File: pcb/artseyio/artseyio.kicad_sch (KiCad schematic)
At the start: 17 parts, among them J1 USB_C16PIN, J2 RST, SW1 SW_MEC_5G, SW2 SW_MEC_5G, SW3 SW_MEC_5G, SW4 SW_MEC_5G, SW5 SW_MEC_5G, SW6 SW_MEC_5G, SW7 SW_MEC_5G, SW8 SW_MEC_5G, U3 CH552G

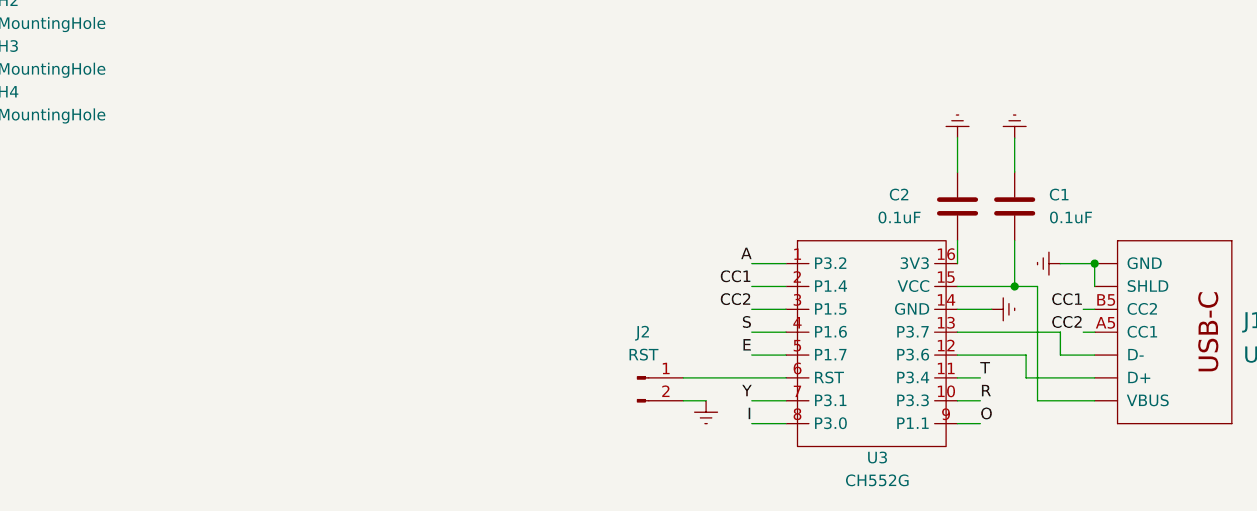
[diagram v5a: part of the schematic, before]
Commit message: Filled out v1.1 design with boot jumper and correct cc line pulldowns.
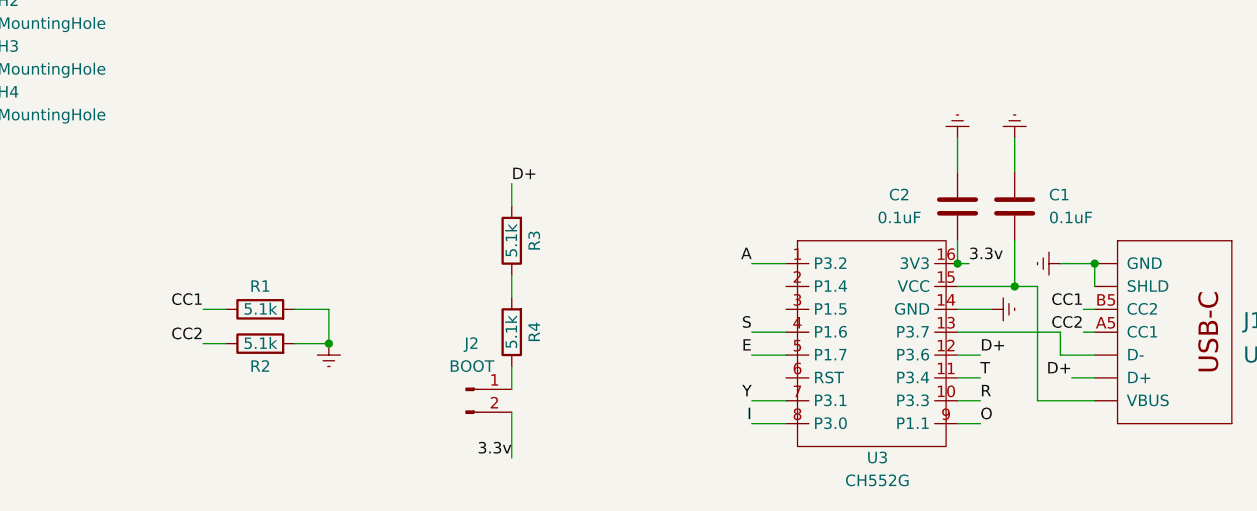
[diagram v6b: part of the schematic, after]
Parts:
- added R1, R2, R3, R4: 5.1k, Resistor_SMD:R_0805_2012Metric, symbol Device:R
- J2: value RST -> BOOT
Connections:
- net CC1: now also R1.1; no longer U3.2 (P1.4)
- net CC2: now also R2.1; no longer U3.3 (P1.5)
- net Earth: now also R1.2, R2.2; no longer J2.2 (Pin_2)
- net at J2.1 (Pin_1): now also R4.1; no longer U3.6 (RST)
- net D+: now reaches J1.A6 (D+), J1.B6 (D+), U3.12 (P3.6)
- net D+: now also R3.2
- net 3.3v: now reaches C2.2, U3.16 (3V3)
- net 3.3v: now also J2.2 (Pin_2)
- new net: R3.1, R4.2

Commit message: Reverted PCB also.
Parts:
- removed R1, R2, R3, R4: 5.1k, Resistor_SMD:R_0805_2012Metric, symbol Device:R
- J2: value BOOT -> RST
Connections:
- net CC1: now also U3.2 (P1.4)
- net CC2: now also U3.3 (P1.5)
- net Earth: now also J2.2 (Pin_2)
- net at J2.1 (Pin_1): now also U3.6 (RST)
- net 3.3v: no longer names the net of C2.2, U3.16 (3V3)
- net 3.3v: no longer J2.2 (Pin_2)
- net D+: no longer names the net of J1.A6 (D+), J1.B6 (D+), U3.12 (P3.6)
